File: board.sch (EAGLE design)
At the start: 43 parts, among them IC3 MCP23008/SO, J11 AUDIO_JACK_TRRSSMD_RA, J13 AUDIO_JACK_TRRSSMD_RA, J2 455-1750-1-ND, J3 AUDIO_JACK_TRRSSMD_RA, J4 AUDIO_JACK_TRRSSMD_RA, J8 XF2E-2015-1, J9 MOLEX_INC_105027-0001MOLEX_IN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

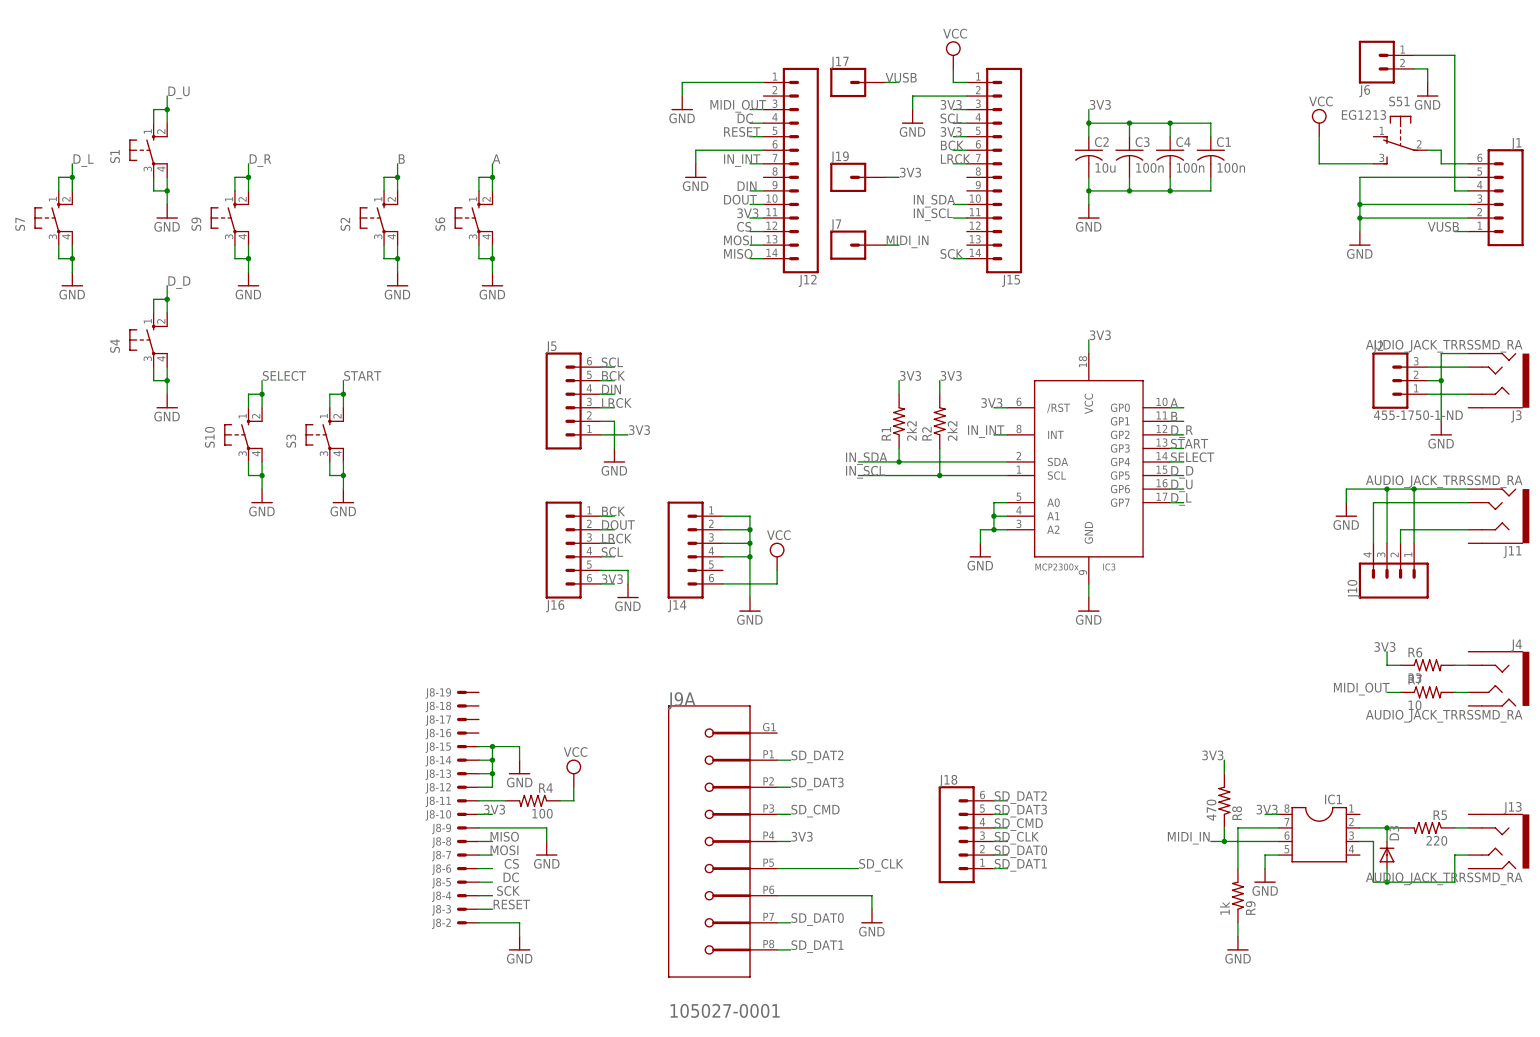
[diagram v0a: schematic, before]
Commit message: pcb fixes
-added an option for the LCD backlight to be adjusted in the device menu
-changed the sd card slot, now its possible to run the device without an sd card
-changed the case filename - the case probably has to be updated due to the new sd card slot
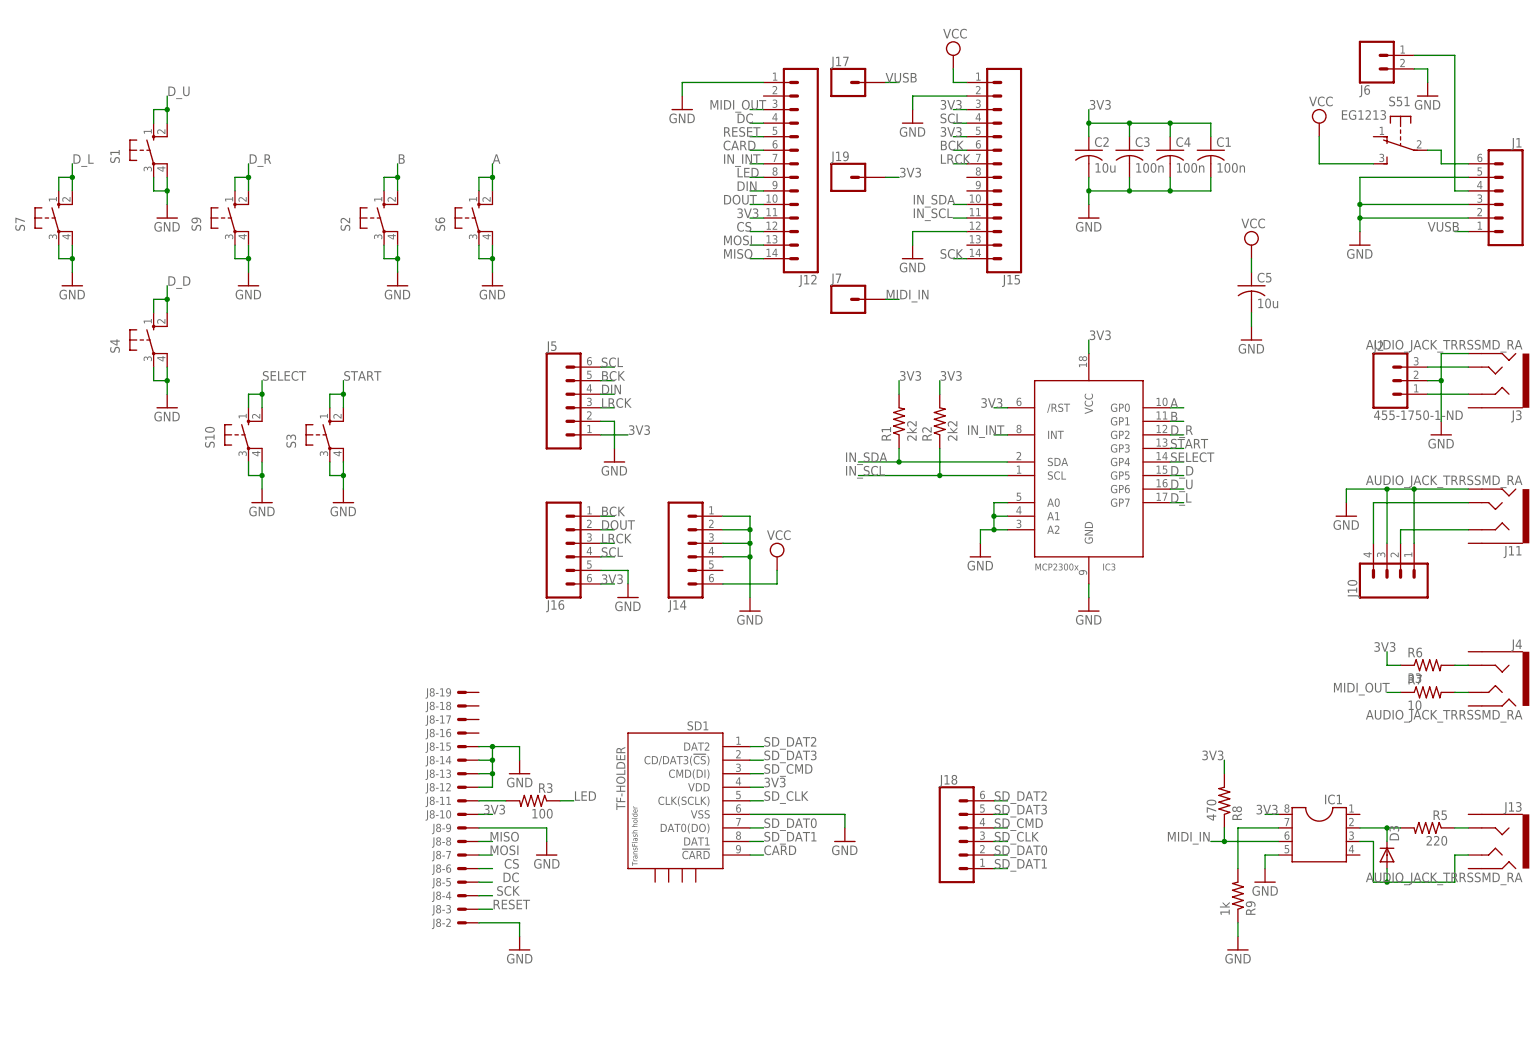
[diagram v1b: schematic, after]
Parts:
- removed J9: MOLEX_INC_105027-0001MOLEX_INC_105027-0001_0_0, Molex Inc - 105027-0001:MOLEX_INC_105027-0001MOLEX_INC_105027-0001_0_0
- added C5: 10u, rcl:C-USC0805
- added SD1: TF-HOLDER, sd-mmc:TF-HOLDER
- renumbered R4 to R3
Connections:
- new net CARD: J12.6, SD1.!CARD
- new net LED: J12.8, R3.1
- net 3V3: now also SD1.VDD; no longer J9A.VDD
- net GND: now also C5.2, J15.12, SD1.VSS; no longer J12.6, J9A.VSS
- net SD_CLK: now also SD1.CLK(SCLK); no longer J9A.CLK
- net SD_CMD: now also SD1.CMD(DI); no longer J9A.CMD
- net SD_DAT0: now also SD1.DAT0(DO); no longer J9A.DAT0
- net SD_DAT1: now also SD1.DAT1; no longer J9A.DAT1
- net SD_DAT2: now also SD1.DAT2; no longer J9A.DAT2
- net SD_DAT3: now also SD1.CD/DAT3(!CS!); no longer J9A.CD/DAT3
- net VCC: now also C5.1; no longer R3.1
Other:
- moved on the sheet: J7

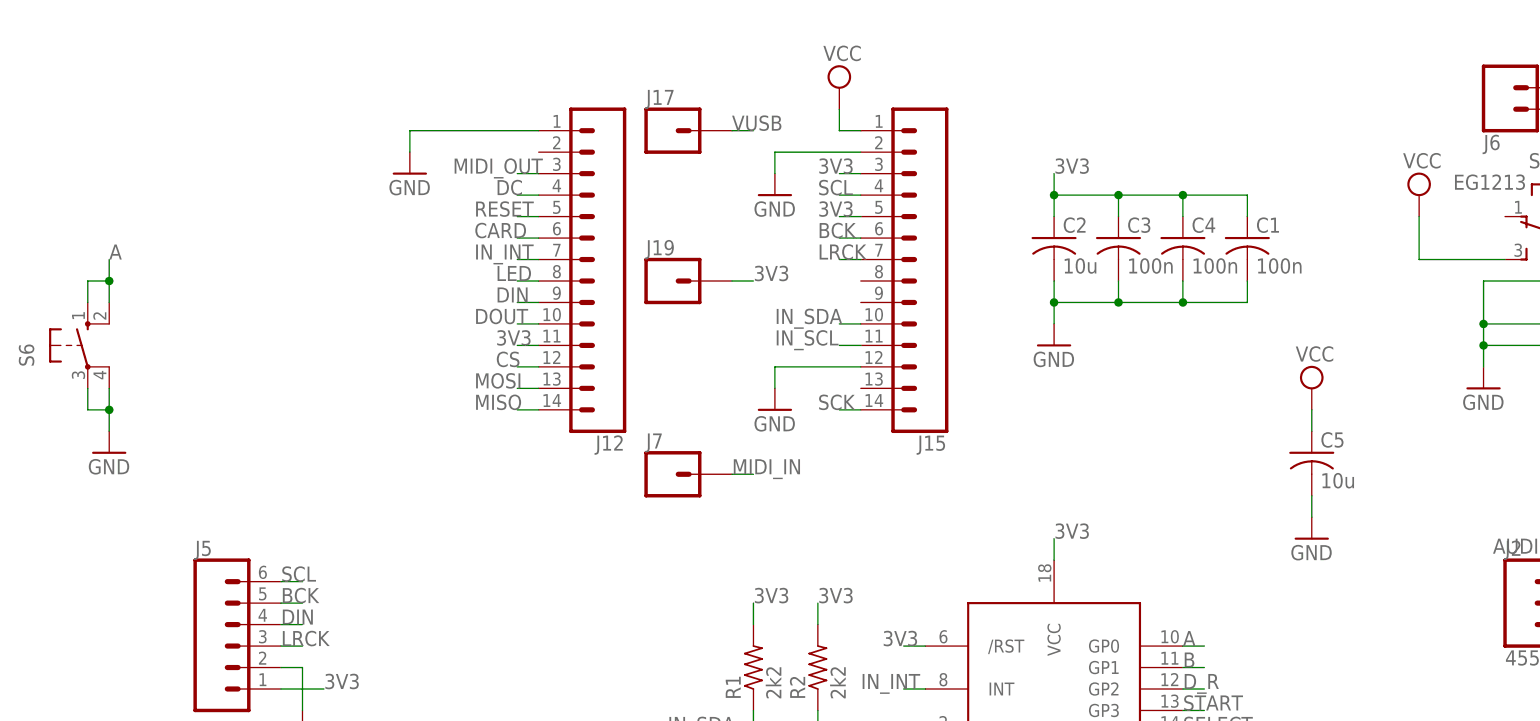
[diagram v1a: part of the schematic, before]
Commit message: small pcb fix
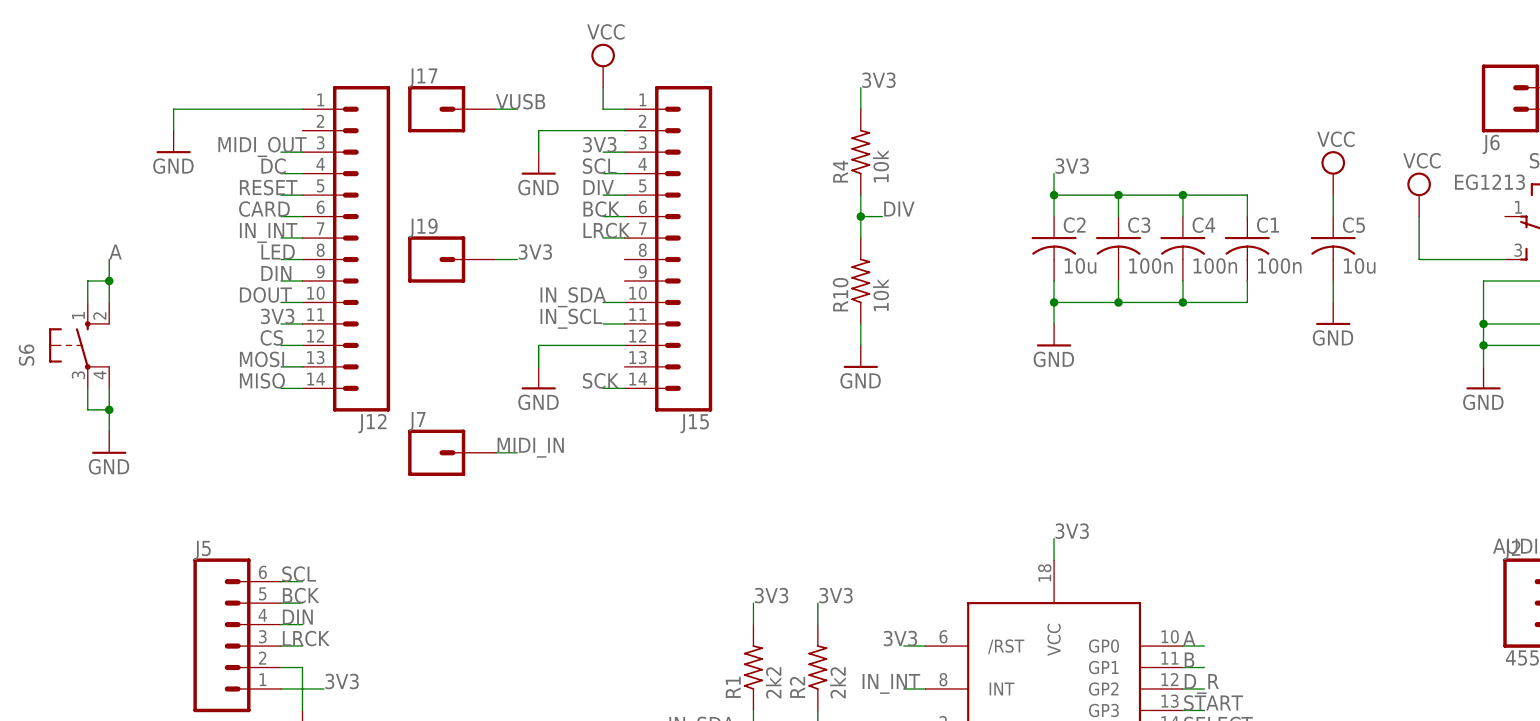
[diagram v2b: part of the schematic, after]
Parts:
- added R10, R4: 10k, rcl:R-US_R0805
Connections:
- new net DIV: J15.5, R10.2, R4.1
- net 3V3: now also R4.2; no longer J15.5
- net GND: now also R10.1
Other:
- moved on the sheet: C5, J12, J15, J17, J19, J7

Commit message: pcb update
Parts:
- removed R10, R4: 10k, rcl:R-US_R0805
- removed R3: 100, rcl:R-US_R0805
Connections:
- removed net DIV: J15.5, R10.2, R4.1
- removed net N$1: J8-11.MS, R3.2
- net 3V3: now also J15.5; no longer R4.2
- net GND: no longer R10.1
- net LED: now also J8-11.MS; no longer R3.1
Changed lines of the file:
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@@
 <part name="GND22" library="supply1" deviceset="GND" device=""/>
 <part name="C5" library="rcl" deviceset="C-US" device="C0805" value="10u"/>
-<part name="R3" library="rcl" deviceset="R-US_" device="R0805" value="100"/>
 <part name="GND23" library="supply1" deviceset="GND" device=""/>
 <part name="SD1" library="sd-mmc" deviceset="TF-HOLDER" device=""/>
-<part name="R4" library="rcl" deviceset="R-US_" device="R0805" value="10k"/>
-<part name="R10" library="rcl" deviceset="R-US_" device="R0805" value="10k"/>
-<part name="GND11" library="supply1" deviceset="GND" device=""/>
 </parts>
 <sheets>
@@
 <instance part="C5" gate="G$1" x="238.76" y="180.34"/>
 <instance part="J8" gate="-11" x="88.9" y="58.42" rot="R180"/>
-<instance part="R3" gate="G$1" x="101.6" y="58.42" rot="MR0"/>
 <instance part="GND23" gate="1" x="144.78" y="162.56"/>
 <instance part="SD1" gate="G$1" x="129.54" y="58.42" rot="MR0"/>
-<instance part="R4" gate="G$1" x="182.88" y="190.5" rot="R90"/>
-<instance part="R10" gate="G$1" x="182.88" y="175.26" rot="R90"/>
-<instance part="GND11" gate="1" x="182.88" y="165.1"/>
 </instances>
 <busses>
@@
 <pinref part="GND23" gate="1" pin="GND"/>
 </segment>
-<segment>
-<pinref part="R10" gate="G$1" pin="1"/>
-<wire x1="182.88" y1="170.18" x2="182.88" y2="167.64" width="0.1524" layer="91"/>
-<pinref part="GND11" gate="1" pin="GND"/>
-</segment>
 </net>
 <net name="VCC" class="0">
@@
 </segment>
 <segment>
-<pinref part="R4" gate="G$1" pin="2"/>
-<wire x1="182.88" y1="198.12" x2="182.88" y2="195.58" width="0.1524" layer="91"/>
-<label x="182.88" y="198.12" size="1.778" layer="95"/>
+<pinref part="J15" gate="G$1" pin="5"/>
+<wire x1="154.94" y1="185.42" x2="152.4" y2="185.42" width="0.1524" layer="91"/>
+<label x="149.86" y="185.42" size="1.778" layer="95"/>
 </segment>
 </net>
@@
 </segment>
 <segment>
-<pinref part="R3" gate="G$1" pin="1"/>
-<wire x1="106.68" y1="58.42" x2="109.22" y2="58.42" width="0.1524" layer="91"/>
-<label x="109.22" y="58.42" size="1.778" layer="95"/>
+<label x="93.98" y="58.42" size="1.778" layer="95"/>
+<pinref part="J8" gate="-11" pin="MS"/>
+<wire x1="91.44" y1="58.42" x2="93.98" y2="58.42" width="0.1524" layer="91"/>
 </segment>
 </net>
@@
 </segment>
 </net>
-<net name="N$1" class="0">
-<segment>
-<pinref part="J8" gate="-11" pin="MS"/>
-<wire x1="91.44" y1="58.42" x2="96.52" y2="58.42" width="0.1524" layer="91"/>
-<pinref part="R3" gate="G$1" pin="2"/>
-</segment>
-</net>
 <net name="CARD" class="0">
 <segment>
@@
 </segment>
 </net>
-<net name="DIV" class="0">
-<segment>
-<pinref part="J15" gate="G$1" pin="5"/>
-<wire x1="154.94" y1="185.42" x2="152.4" y2="185.42" width="0.1524" layer="91"/>
-<label x="149.86" y="185.42" size="1.778" layer="95"/>
-</segment>
-<segment>
-<pinref part="R4" gate="G$1" pin="1"/>
-<pinref part="R10" gate="G$1" pin="2"/>
-<wire x1="182.88" y1="185.42" x2="182.88" y2="182.88" width="0.1524" layer="91"/>
-<wire x1="182.88" y1="182.88" x2="182.88" y2="180.34" width="0.1524" layer="91"/>
-<wire x1="182.88" y1="182.88" x2="185.42" y2="182.88" width="0.1524" layer="91"/>
-<junction x="182.88" y="182.88"/>
-<label x="185.42" y="182.88" size="1.778" layer="95"/>
-</segment>
-</net>
